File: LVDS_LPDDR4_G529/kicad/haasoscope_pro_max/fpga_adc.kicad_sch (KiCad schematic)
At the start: 0 parts

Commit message: Aligned schematics, sort of
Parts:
- added IC1: ADC12DL500ACF_Aligned, ADC12DL:BGA256C100P16X16_1700X1700X331, symbol Aligned_Peripheral_Symbols:ADC12DL500ACF_Aligned
- added U3: Ti90G529_Functions, G529:BGA-529_23x23_19.0x19.0mm, symbol Ti90G529_Functions:Ti90G529_Functions

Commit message: Aligned schematics, sort of
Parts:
- removed unit 5 of IC1
- added unit 4 of U3
- IC1: footprint ADC12DL:BGA256C100P16X16_1700X1700X331 -> BGA256C100P16X16_1700X1700X331
- U3: footprint G529:BGA-529_23x23_19.0x19.0mm -> haasoscope_pro_adc_fpga_board:BGA-529_23x23_19.0x19.0mm
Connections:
- net at U3.B1 (lvds_rx4_11): now also IC1.M15 (DD10+)
- net at U3.C1 (lvds_rx4_11_N): now also IC1.M16 (DD10-)
- net at U3.C2 (lvds_rx3_1_N): now also IC1.T10 (DB0-)
- net at U3.C3 (lvds_rx3_1): now also IC1.T9 (DB0+)
- net at U3.D2 (lvds_rx4_13): now also IC1.J15 (DDSTR+)
- net at U3.D3 (lvds_rx4_13_N): now also IC1.J16 (DDSTR-)
- net at U3.E1 (lvds_rx3_12): now also IC1.L11 (DB11+)
- net at U3.E4 (lvds_rx4_12): now also IC1.L15 (DD11+)
- net at U3.F1 (lvds_rx3_12_N): now also IC1.L12 (DB11-)
- net at U3.F3 (lvds_rx4_5): now also IC1.M13 (DD4+)
- net at U3.F4 (lvds_rx4_12_N): now also IC1.L16 (DD11-)
- net at U3.G3 (lvds_rx4_5_N): now also IC1.M14 (DD4-)
- net at U3.H2 (lvds_rx4_4): now also IC1.N13 (DD3+)
- net at U3.H3 (lvds_rx4_4_N): now also IC1.N14 (DD3-)
- net at U3.H5 (lvds_rx4_8): now also IC1.R15 (DD7+)
- net at U3.J2 (lvds_rx4_2_N): now also IC1.R14 (DD1-)
- net at U3.J3 (lvds_rx4_2): now also IC1.R13 (DD1+)
- net at U3.J4 (lvds_rx4_7_N): now also IC1.K14 (DD6-)
- net at U3.J5 (lvds_rx4_8_N): now also IC1.R16 (DD7-)
- net at U3.J6 (lvds_rx4_10_N): now also IC1.N16 (DD9-)
- net at U3.J7 (lvds_rx4_10): now also IC1.N15 (DD9+)
- net at U3.K1 (lvds_rx3_11): now also IC1.M11 (DB10+)
- net at U3.K3 (lvds_rx4_1_N): now also IC1.T14 (DD0-)
- net at U3.K4 (lvds_rx4_7): now also IC1.K13 (DD6+)
- net at U3.K6 (lvds_rx4_9): now also IC1.P15 (DD8+)
- net at U3.L1 (lvds_rx3_11_N): now also IC1.M12 (DB10-)
- net at U3.L2 (lvds_rx3_10): now also IC1.N11 (DB9+)
- net at U3.L3 (lvds_rx4_1): now also IC1.T13 (DD0+)
- net at U3.L4 (lvds_rx4_3): now also IC1.P13 (DD2+)
- net at U3.L5 (lvds_rx4_3_N): now also IC1.P14 (DD2-)
- net at U3.L6 (lvds_rx4_9_N): now also IC1.P16 (DD8-)
- net at U3.L7 (lvds_rx4_6): now also IC1.L13 (DD5+)
- net at U3.L8 (lvds_rx4_6_N): now also IC1.L14 (DD5-)
- net at U3.M2 (lvds_rx3_10_N): now also IC1.N12 (DB9-)
- net at U3.M4 (lvds_rx3_9_N): now also IC1.P12 (DB8-)
- net at U3.M6 (lvds_rx3_13): now also IC1.J9 (DBSTR+)
- net at U3.M7 (lvds_rx3_13_N): now also IC1.J10 (DBSTR-)
- net at U3.N1 (lvds_rx3_8): now also IC1.R11 (DB7+)
- net at U3.N2 (lvds_rx3_8_N): now also IC1.R12 (DB7-)
- net at U3.N3 (lvds_rx3_7): now also IC1.T11 (DB6+)
- net at U3.N4 (lvds_rx3_9): now also IC1.P11 (DB8+)
- net at U3.N5 (lvds_rx3_6): now also IC1.L9 (DB5+)
- net at U3.N6 (lvds_rx3_6_N): now also IC1.L10 (DB5-)
- net at U3.P1 (lvds_rx3_4): now also IC1.N9 (DB3+)
- net at U3.P3 (lvds_rx3_7_N): now also IC1.T12 (DB6-)
- net at U3.P5 (lvds_rx3_5): now also IC1.M9 (DB4+)
- net at U3.P6 (lvds_rx3_5_N): now also IC1.M10 (DB4-)
- net at U3.P7 (lvds_rx3_3_N): now also IC1.P10 (DB2-)
- net at U3.P8 (lvds_rx3_3): now also IC1.P9 (DB2+)
- net at U3.R1 (lvds_rx3_4_N): now also IC1.N10 (DB3-)
- net at U3.R2 (lvds_rx3_2): now also IC1.R9 (DB1+)
- net at U3.R3 (lvds_rx3_2_N): now also IC1.R10 (DB1-)
- net at U3.B22 (lvds_rx2_11_N): now also IC1.E16 (DC10-)
- net at U3.B23 (lvds_rx2_11): now also IC1.E15 (DC10+)
- net at U3.E20 (lvds_rx1_1_N): now also IC1.A10 (DA0-)
- net at U3.E21 (lvds_rx1_1): now also IC1.A9 (DA0+)
- net at U3.E22 (lvds_rx2_4_N): now also IC1.D14 (DC3-)
- net at U3.E23 (lvds_rx2_4): now also IC1.D13 (DC3+)
- net at U3.F21 (lvds_rx2_7_N): now also IC1.G14 (DC6-)
- net at U3.F23 (lvds_rx2_2): now also IC1.B13 (DC1+)
- net at U3.G20 (lvds_rx2_13_N): now also IC1.H16 (DCSTR-)
- net at U3.G21 (lvds_rx2_7): now also IC1.G13 (DC6+)
- net at U3.G22 (lvds_rx1_12): now also IC1.F11 (DA11+)
- net at U3.G23 (lvds_rx2_2_N): now also IC1.B14 (DC1-)
- net at U3.H20 (lvds_rx2_13): now also IC1.H15 (DCSTR+)
- net at U3.H22 (lvds_rx1_12_N): now also IC1.F12 (DA11-)
- net at U3.J17 (lvds_rx2_10_N): now also IC1.D16 (DC9-)
- net at U3.J18 (lvds_rx2_10): now also IC1.D15 (DC9+)
- net at U3.J20 (lvds_rx2_5): now also IC1.E13 (DC4+)
- net at U3.J21 (lvds_rx2_5_N): now also IC1.E14 (DC4-)
- net at U3.K17 (lvds_rx2_12_N): now also IC1.F16 (DC11-)
- net at U3.K18 (lvds_rx2_12): now also IC1.F15 (DC11+)
- net at U3.K19 (lvds_rx2_8_N): now also IC1.B16 (DC7-)
- net at U3.K20 (lvds_rx2_8): now also IC1.B15 (DC7+)
- net at U3.K21 (lvds_rx2_1_N): now also IC1.A14 (DC0-)
- net at U3.L16 (lvds_rx2_3): now also IC1.C13 (DC2+)
- net at U3.L17 (lvds_rx2_6_N): now also IC1.F14 (DC5-)
- net at U3.L18 (lvds_rx2_6): now also IC1.F13 (DC5+)
- net at U3.L19 (lvds_rx2_9_N): now also IC1.C16 (DC8-)
- net at U3.L20 (lvds_rx2_9): now also IC1.C15 (DC8+)
- net at U3.L21 (lvds_rx2_1): now also IC1.A13 (DC0+)
- net at U3.L22 (lvds_rx1_7_N): now also IC1.A12 (DA6-)
- net at U3.L23 (lvds_rx1_7): now also IC1.A11 (DA6+)
- net at U3.M16 (lvds_rx2_3_N): now also IC1.C14 (DC2-)
- net at U3.M18 (lvds_rx1_13_N): now also IC1.H10 (DASTR-)
- net at U3.M19 (lvds_rx1_13): now also IC1.H9 (DASTR+)
- net at U3.M21 (lvds_rx1_11): now also IC1.E11 (DA10+)
- net at U3.M22 (lvds_rx1_11_N): now also IC1.E12 (DA10-)
- net at U3.N16 (lvds_rx1_9): now also IC1.C11 (DA8+)
- net at U3.N17 (lvds_rx1_9_N): now also IC1.C12 (DA8-)
- net at U3.N18 (lvds_rx1_10_N): now also IC1.D12 (DA9-)
- net at U3.N19 (lvds_rx1_10): now also IC1.D11 (DA9+)
- net at U3.N20 (lvds_rx1_8): now also IC1.B11 (DA7+)
- net at U3.N21 (lvds_rx1_8_N): now also IC1.B12 (DA7-)
- net at U3.N22 (lvds_rx1_5): now also IC1.E9 (DA4+)
- net at U3.N23 (lvds_rx1_5_N): now also IC1.E10 (DA4-)
- net at U3.P18 (lvds_rx1_6): now also IC1.F9 (DA5+)
- net at U3.P19 (lvds_rx1_6_N): now also IC1.F10 (DA5-)
- net at U3.P20 (lvds_rx1_4_N): now also IC1.D10 (DA3-)
- net at U3.P21 (lvds_rx1_4): now also IC1.D9 (DA3+)
- net at U3.P23 (lvds_rx1_2_N): now also IC1.B10 (DA1-)
- net at U3.R18 (lvds_rx1_3): now also IC1.C9 (DA2+)
- net at U3.R19 (lvds_rx1_3_N): now also IC1.C10 (DA2-)
- net at U3.R23 (lvds_rx1_2): now also IC1.B9 (DA1+)
- new net: IC1.K15 (DDCLK+), U3.G1 (lvds_rx_bottom_clkin4)
- new net: IC1.K16 (DDCLK-), U3.G2 (lvds_rx_bottom_clkin4_N)
- new net: IC1.G9 (DACLK+), U3.J22 (lvds_rx_top_clkin1)
- new net: IC1.G10 (DACLK-), U3.J23 (lvds_rx_top_clkin1_N)
- new net: IC1.G16 (DCCLK-), U3.R21 (lvds_rx_top_clkin2_N)
- new net: IC1.G15 (DCCLK+), U3.R22 (lvds_rx_top_clkin2)
- new net: IC1.K9 (DBCLK+), U3.R4 (lvds_rx_bottom_clkin3)
- new net: IC1.K10 (DBCLK-), U3.R5 (lvds_rx_bottom_clkin3_N)
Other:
- moved on the sheet: U3B, U3C

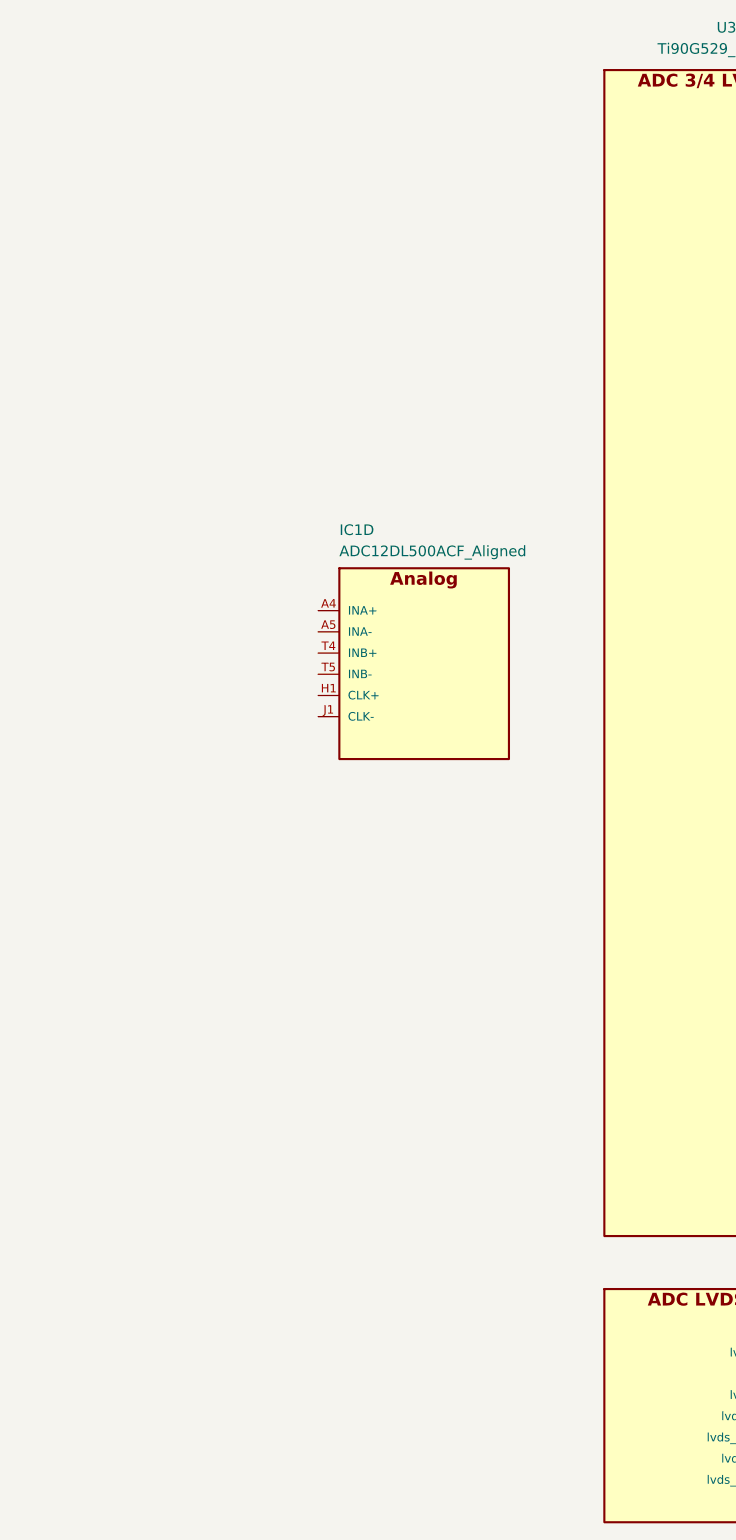
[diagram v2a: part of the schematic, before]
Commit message: Aligned schematics, better
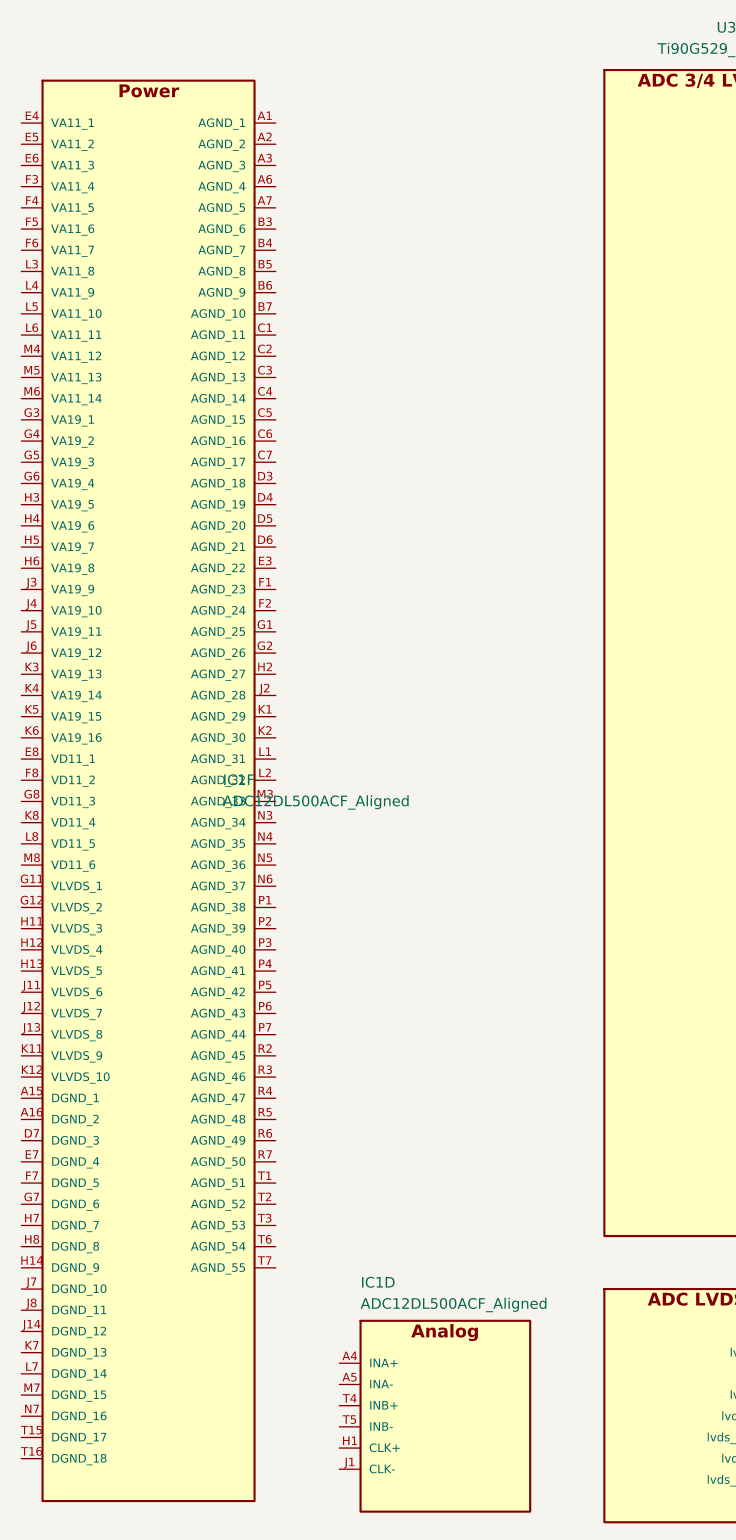
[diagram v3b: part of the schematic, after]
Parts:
- added unit 6 of IC1
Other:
- moved on the sheet: IC1D
